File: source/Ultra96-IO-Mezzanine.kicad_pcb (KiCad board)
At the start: 2 copper layers, 85 x 54 mm, 58 parts, among them J1 USB_C_Receptacle_USB2.0, J2 Conn_01x08_Female, J3 USB_C_Receptacle_USB2.0, P1 CONN_02X20, P2 CONN_02X30, P3 CONN_02X20, Q1 STL6P3LLH6, SW1 SW_SP3T, SW2 PWR_BTN, SW3 RST_BTN, U2 CP2102N-A01-GQFN24, U3 TXS0108EPW, U4 STUSB4500QTR, U5 TXS0108EPW, U6 TXS0108EPW, U7 TXS0108EPW

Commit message: maybe working now?
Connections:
- Q1 pad 5_6_7_8: SYS_DCIN -> (no net)
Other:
- board text added: "v1.0.0"
- board text removed: "RevA"

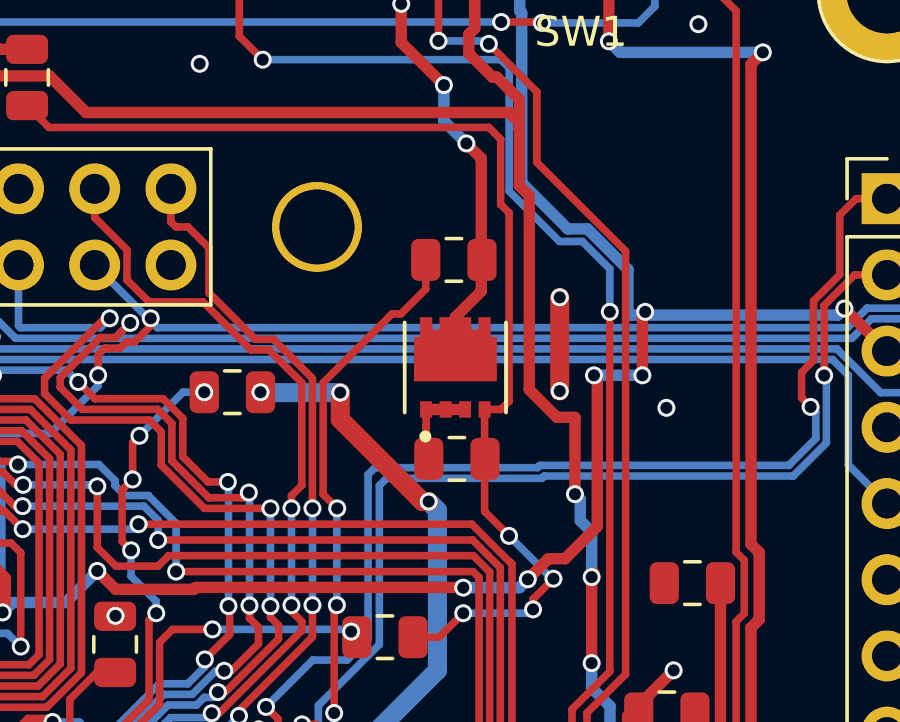
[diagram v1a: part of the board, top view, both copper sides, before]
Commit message: Updated workflows and fixed DRC issues
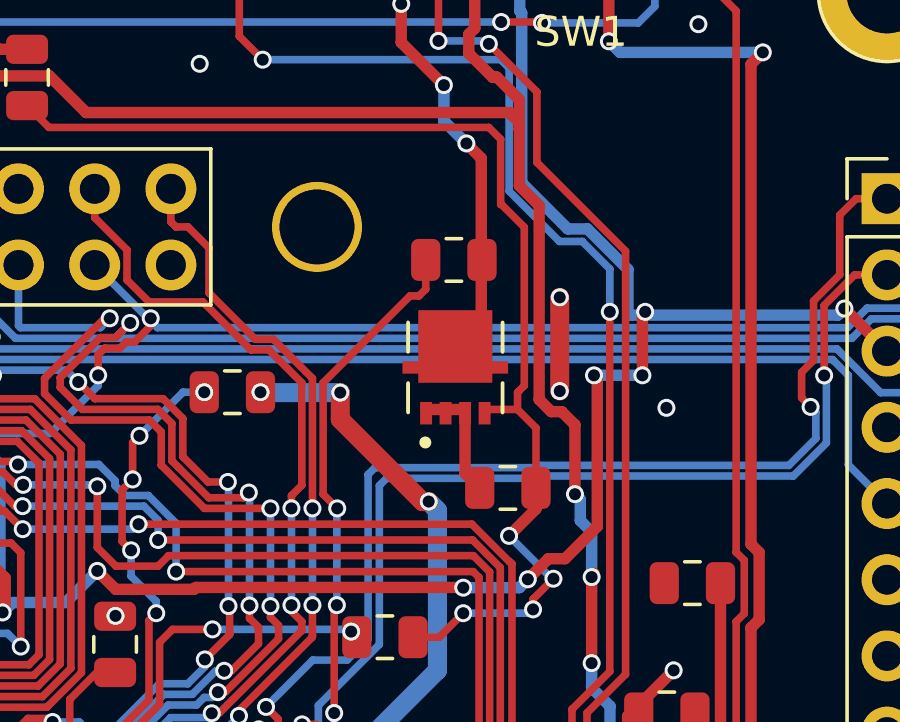
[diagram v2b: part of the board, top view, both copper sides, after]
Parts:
- Q1: footprint snapeda:TRANS_STL6P3LLH6 -> STL6P3LLH6:TRANS_STL6P3LLH6
- moved R7 1.95 mm to (168.4, 120.5)
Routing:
- net Net-(Q1-Pad4): track 38.3 -> 39.4 mm
- net Net-(Q1-Pad1): track 2.98 -> 3.99 mm

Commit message: testing CI tweak
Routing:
- net +5V: track 156.5 -> 155.2 mm, vias 9 -> 11
- net Net-(Q1-Pad4): vias 4 -> 6
